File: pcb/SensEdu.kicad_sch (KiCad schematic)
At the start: 30 parts, among them J1 Power, J10 Barrel_Jack_Switch, J13 Conn_02x01, J14 Conn_02x01, J15 Conn_02x01, J16 Conn_02x01, J2 PWM, J3 Analog, J4 PWM, J5 Analog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

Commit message: Progress in pcb routing
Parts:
- removed C3, C37, C38, C56: 10u, Capacitor_SMD:C_0805_2012Metric, symbol Device:C
- removed C36, C4, C55, C57, C8: 100n, Capacitor_SMD:C_0805_2012Metric, symbol Device:C
- removed C7: 1u, Capacitor_SMD:C_0805_2012Metric, symbol Device:C
- removed D1: LED, LED_SMD:LED_0805_2012Metric, symbol Device:LED
- removed FB1, FB2: FerriteBead, Inductor_SMD:L_1206_3216Metric, symbol Device:FerriteBead
- removed J10: Barrel_Jack_Switch, Connector_BarrelJack:BarrelJack_Wuerth_6941xx301002, symbol Connector:Barrel_Jack_Switch
- removed J13, J14, J15, J16: Conn_02x01, Connector_PinSocket_2.54mm:PinSocket_1x02_P2.54mm_Vertical, symbol Connector_Generic:Conn_02x01
- removed JP3: Jumper_3_Bridged12, Connector_PinHeader_2.54mm:PinHeader_1x03_P2.54mm_Vertical, symbol Jumper:Jumper_3_Bridged12
- removed R1: 47, Resistor_SMD:R_0805_2012Metric, symbol Device:R
- removed U12: TLS850C2TE_V33, Package_TO_SOT_SMD:TO-252-4, symbol SensEdu:TLS850C2TEV50ATMA1
- removed U13: NCP1117-2.5_SOT223, Package_TO_SOT_SMD:SOT-223-3_TabPin2, symbol Regulator_Linear:NCP1117-2.5_SOT223
- removed U3: LT1790ACS6-1.25, Package_TO_SOT_SMD:TSOT-23-6, symbol SensEdu:LT1790-2.5_sensedu
- J4: renamed from J7; now not fitted
- renumbered J3 to J1, J5 to J2, J1 to J3, J2 to J5, J4 to J6, J6 to J7
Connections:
- net *2 renamed 3*
- net *3 renamed 4*
- net *4 renamed SE_PWM_1
- net *6 renamed S2
- net *7 renamed S1
- net 37 renamed SE_PWM_2
- net 48 renamed SE_PWM_3
- net 5V0 renamed +5V_ARDUINO
- net A0 renamed OUT_MIC5
- net A1 renamed OUT_MIC6
- net A10 renamed OUT_MIC7
- net A12 renamed DAC0
- net A13 renamed DAC1
- net A2 renamed OUT_MIC2
- net A3 renamed OUT_MIC1
- net A5: no longer names the net of J1.6 (Pin_6)
- net A6: no longer names the net of J1.7 (Pin_7)
- net A7: no longer names the net of J1.8 (Pin_8)
- net A8 renamed OUT_MIC3
- net A9 renamed OUT_MIC4
- net Microphones/MIC7_OUT renamed OUT_MIC8
- net SCL/21 renamed SCL
- net SDA/20 renamed SDA
- no-connect marks 69 -> 63
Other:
- sheet Pressure Sensor renamed Sensors
- added sheet Power (power.kicad_sch)
- sheet Sensors: file Pressure_sensor.kicad_sch -> Sensors.kicad_sch
- sheet Sensors ports: added SCL, SDA; removed SCL1, SDA1
- sheet Speakers ports: added none; removed PWM_2, PWM_3
- note removed: "LOW DROPOUT VOLTAGE REFERENCE 3.3V->1.25V"
- note removed: "POWER"
- moved on the sheet: J1, J2, J3, J5, J6, J7

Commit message: in works
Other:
- title: SensEdu 0.7 -> SensEdu 0.9
- moved on the sheet: J1, J2, J3, J4, J5, J6, J7

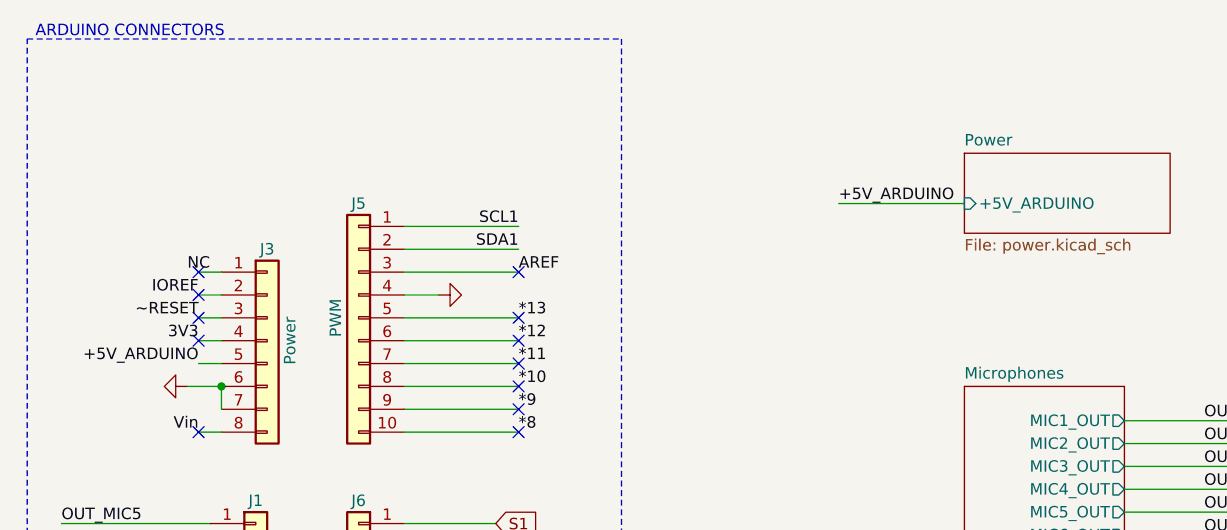
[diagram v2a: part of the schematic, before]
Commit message: fix: PCB final fixes
Added simulation for dc offset after ac coupling
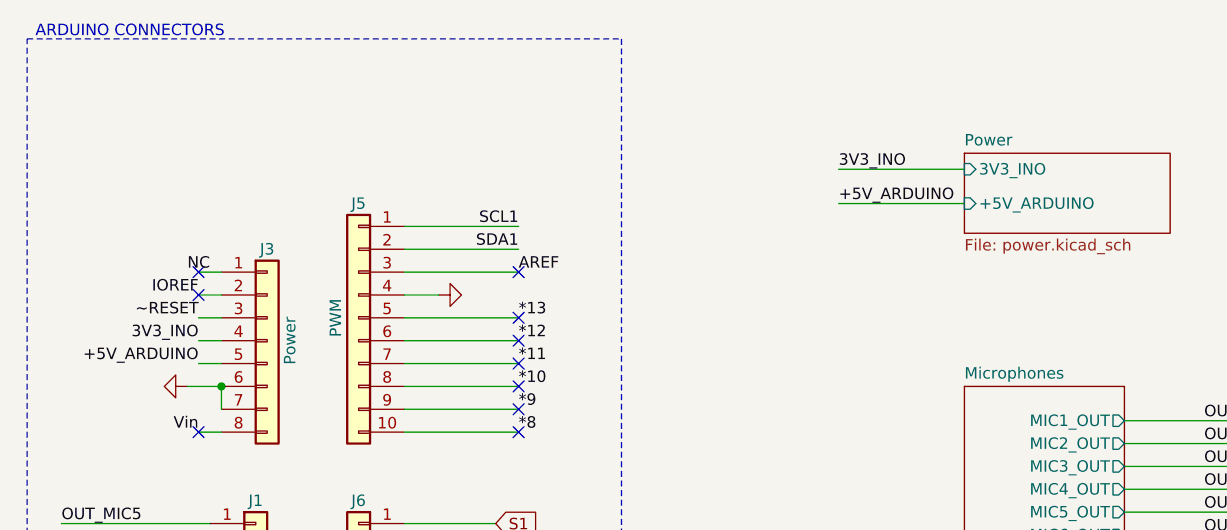
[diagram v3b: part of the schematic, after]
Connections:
- net 3V3 renamed 3V3_INO
- no-connect marks 63 -> 61
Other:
- sheet Power ports: added 3V3_INO; removed none
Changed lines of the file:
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@@
-	)
-	(no_connect
-		(at 81.28 60.96)
 	)
 	(no_connect
@@
 	)
 	(no_connect
-		(at 81.28 58.42)
-	)
-	(no_connect
 		(at 82.55 121.92)
 	)
@@
 		(pts
 			(xy 81.28 60.96) (xy 83.82 60.96)
+		)
+		(stroke
+			(width 0)
+			(type default)
+		)
+	)
+	(wire
+		(pts
+			(xy 152.4 41.91) (xy 166.37 41.91)
 		)
 		(stroke
@@
 		)
 	)
+	(label "3V3_INO"
+		(at 152.4 41.91 0)
+		(effects
+			(font
+				(size 1.27 1.27)
+			)
+			(justify left bottom)
+		)
+	)
 	(label "33"
 		(at 101.6 157.48 90)
@@
 		)
 	)
-	(label "3V3"
+	(label "3V3_INO"
 		(at 81.28 60.96 180)
 		(effects
@@
 			(effects
 				(font
+					(size 1.27 1.27)
+				)
+				(justify left)
+			)
+		)
+		(pin "3V3_INO" input
+			(at 166.37 41.91 180)
+			(effects
+				(font

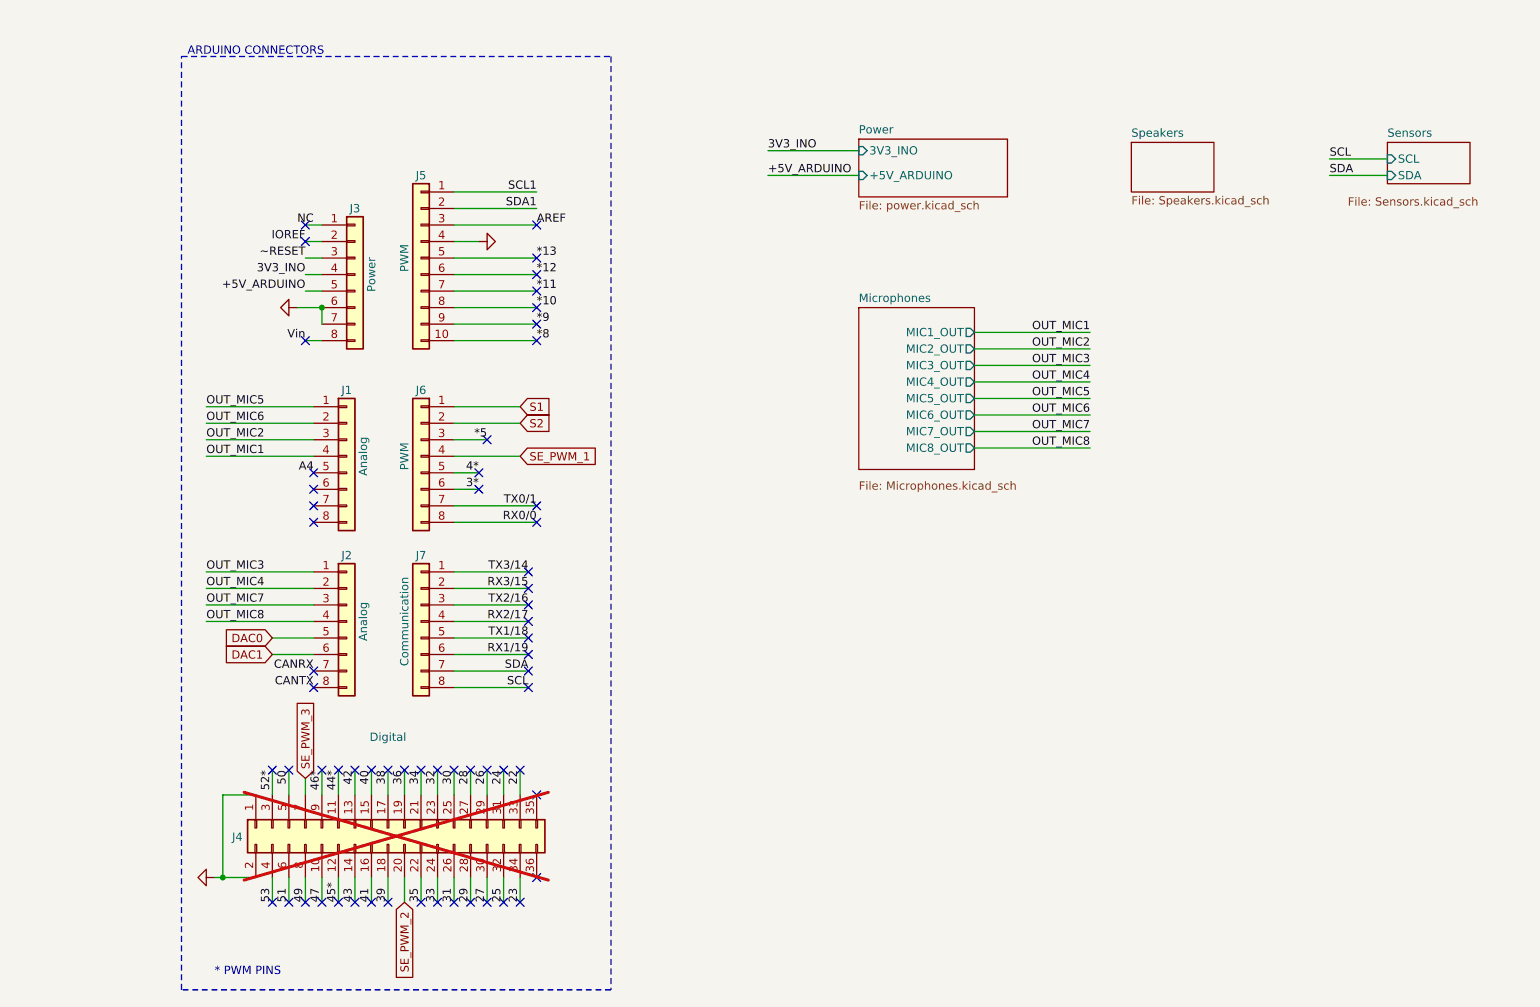
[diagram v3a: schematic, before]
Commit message: feat: Redraw PCB layout
- Change supply polarity and pin numbers of ADA4511
- Change cap of switches to 100n to reduce bom
- Change supply of sensors to unison 3.3V
- Rearrange mic and amps pins
- Add mountains
- Add Infineon logo
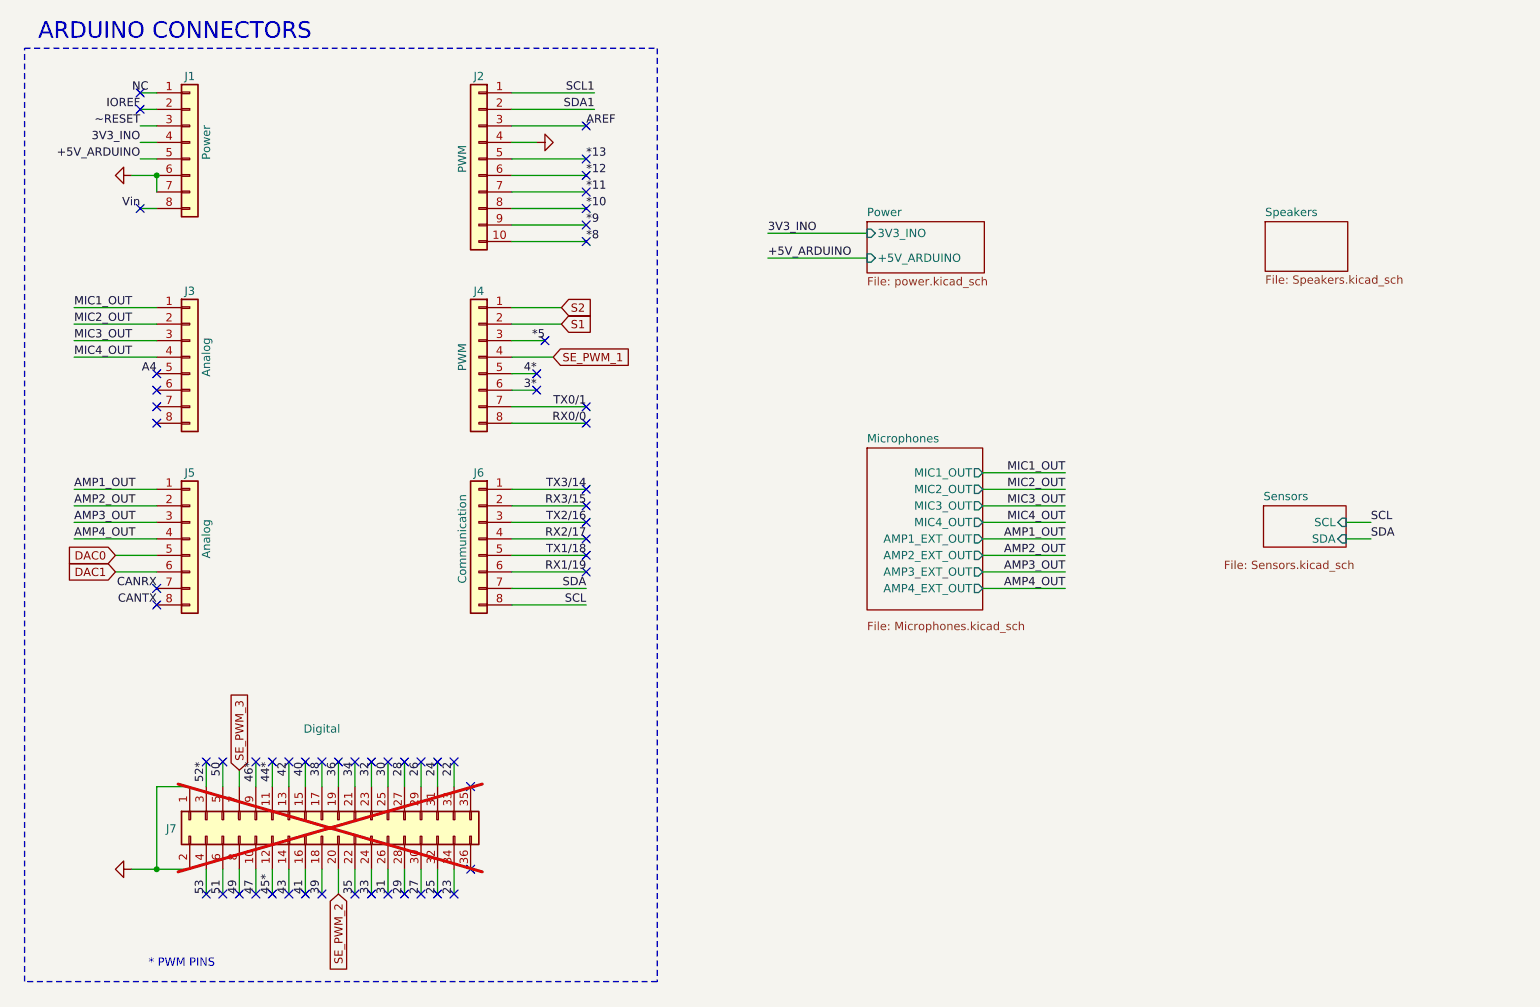
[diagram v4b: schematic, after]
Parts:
- J1: renamed from J3; symbol Connector_Generic:Conn_01x08 -> SensEdu:Conn_01x08
- J2: renamed from J5; symbol Connector_Generic:Conn_01x10 -> SensEdu:Conn_01x10
- J3: renamed from J1; symbol Connector_Generic:Conn_01x08 -> SensEdu:Conn_01x08
- J4: renamed from J6; symbol Connector_Generic:Conn_01x08 -> SensEdu:Conn_01x08
- J5: renamed from J2; symbol Connector_Generic:Conn_01x08 -> SensEdu:Conn_01x08
- J6: renamed from J7; symbol Connector_Generic:Conn_01x08 -> SensEdu:Conn_01x08
- J7: renamed from J4; symbol Connector_Generic:Conn_02x18_Odd_Even -> SensEdu:Conn_02x18_Odd_Even
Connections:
- net S1: now also J4.2 (Pin_2); no longer J4.1 (Pin_1)
- net S2: now also J4.1 (Pin_1); no longer J4.2 (Pin_2)
- net OUT_MIC1 renamed MIC4_OUT
- net OUT_MIC2 renamed MIC3_OUT
- net OUT_MIC3 renamed AMP1_OUT
- net OUT_MIC4 renamed AMP2_OUT
- net OUT_MIC5 renamed MIC1_OUT
- net OUT_MIC6 renamed MIC2_OUT
- net OUT_MIC7 renamed AMP3_OUT
- net OUT_MIC8 renamed AMP4_OUT
- no-connect marks 61 -> 59
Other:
- sheet Microphones ports: added AMP1_EXT_OUT, AMP2_EXT_OUT, AMP3_EXT_OUT, AMP4_EXT_OUT; removed MIC5_OUT, MIC6_OUT, MIC7_OUT, MIC8_OUT
- moved on the sheet: J1, J2, J3, J4, J5, J6, J7

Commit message: refactor: Update PDF and information
- Add BOM
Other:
- title: SensEdu 0.9 -> SensEdu
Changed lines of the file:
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@@
 	(paper "A4")
 	(title_block
-		(title "SensEdu 0.9")
-		(date "2025-12-05")
+		(title "SensEdu")
+		(date "2026-02-26")
 		(rev "0.9")
 		(company "Infineon Technologies")

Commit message: feat: Improve PCB design after tests of rev 0.8
- Added new generation of humidity sensor
- New silkscreen information for different components
- Added additional testpoints
- Removed PWM path for ultrasound transmitter
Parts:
- J1, J3, J4, J5, J6: footprint Connector_PinSocket_2.54mm:PinSocket_1x08_P2.54mm_Vertical -> SensEdu:PinSocket_1x08_P2.54mm_Vertical
- J2: footprint Connector_PinSocket_2.54mm:PinSocket_1x10_P2.54mm_Vertical -> SensEdu:PinSocket_1x10_P2.54mm_Vertical
- J7: footprint Connector_PinSocket_2.54mm:PinSocket_2x18_P2.54mm_Vertical -> SensEdu:PinSocket_2x18_P2.54mm_Vertical
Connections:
- net A5: now reaches J3.6 (Pin_6)
- net A6: now reaches J3.7 (Pin_7)
- net A7: now reaches J3.8 (Pin_8)
- net *10 renamed CS
- net *11 renamed COPI
- net *12 renamed CIPO
- net *13 renamed SCK
- net *5 renamed D5
- net *8 renamed SCL2
- net *9 renamed SDA2
- net 3* renamed D2
- net 4* renamed D3
- net S1 renamed D6
- net S2 renamed D7
- net SE_PWM_1 renamed D4
- net SE_PWM_2: no longer names the net of J7.20 (Pin_20)
- net SE_PWM_3: no longer names the net of J7.7 (Pin_7)
- no-connect marks 59 -> 64
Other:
- note removed: "* PWM PINS"
